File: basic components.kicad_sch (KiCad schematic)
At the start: 56 parts, among them U1601 74HC595, U1602 74HC165, U1603 ULN2803A, U1604 ULN2003A

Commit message: added ch340.sch
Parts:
- added Q?: AO3400A, Package_TO_SOT_SMD:SOT-23, symbol Transistor_FET:AO3400A
- D1606: footprint (none) -> Diode_SMD:D_SMA; JLCPCB Part# (none) -> C49264
- D1609: value (none) -> yellow_LED; footprint (none) -> LED_SMD:LED_0805_2012Metric_Pad1.15x1.40mm_HandSolder
- U?: value (none) -> EL817; footprint (none) -> Package_DIP:SMDIP-4_W9.53mm
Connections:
- net data_out: now also U1602.10 (DS)
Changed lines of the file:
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@@
   )
   (no_connect (at 189.23 31.75))
+  (wire (pts (xy 161.29 29.21) (xy 163.83 29.21))
+    (stroke (width 0) (type default) (color 0 0 0 0))
+  )
   (wire (pts (xy 232.41 55.88) (xy 232.41 57.15))
     (stroke (width 0) (type default) (color 0 0 0 0))
@@
       (effects (font (size 1.27 1.27)) (justify right))
     )
-    (property "Footprint" "" (id 2) (at 111.76 50.8 0)
+    (property "Footprint" "Diode_SMD:D_SMA" (id 2) (at 111.76 50.8 0)
       (effects (font (size 1.27 1.27)) hide)
     )
     (property "Datasheet" "~" (id 3) (at 111.76 50.8 0)
+      (effects (font (size 1.27 1.27)) hide)
+    )
+    (property "JLCPCB Part#" "C49264" (id 4) (at 111.76 50.8 90)
       (effects (font (size 1.27 1.27)) hide)
     )
@@
     (pin "1")
   )
+  (symbol (lib_id "Transistor_FET:AO3400A") (at 113.03 154.94 0) (unit 1)
+    (in_bom yes) (on_board yes) (fields_autoplaced)
+    (property "Reference" "Q?" (id 0) (at 118.237 154.1053 0)
+      (effects (font (size 1.27 1.27)) (justify left))
+    )
+    (property "Value" "AO3400A" (id 1) (at 118.237 156.6422 0)
+      (effects (font (size 1.27 1.27)) (justify left))
+    )
+    (property "Footprint" "Package_TO_SOT_SMD:SOT-23" (id 2) (at 118.11 156.845 0)
+      (effects (font (size 1.27 1.27) italic) (justify left) hide)
+    )
+    (property "Datasheet" "http://www.aosmd.com/pdfs/datasheet/AO3400A.pdf" (id 3) (at 113.03 154.94 0)
+      (effects (font (size 1.27 1.27)) (justify left) hide)
+    )
+    (property "JLCPCB Part#" "C20917" (id 4) (at 113.03 154.94 0)
+      (effects (font (size 1.27 1.27)) hide)
+    )
+    (pin "1")
+    (pin "2")
+    (pin "3")
+  )
   (symbol (lib_id "74xx:74HC595") (at 232.41 36.83 0) (unit 1)
     (in_bom yes) (on_board yes) (fields_autoplaced)
@@
     (in_bom yes) (on_board yes) (fields_autoplaced)
     (property "Reference" "U?" (id 0) (at 96.52 148.7002 0))
-    (property "Value" "" (id 1) (at 96.52 151.2371 0))
-    (property "Footprint" "" (id 2) (at 91.44 161.29 0)
+    (property "Value" "EL817" (id 1) (at 96.52 151.2371 0))
+    (property "Footprint" "Package_DIP:SMDIP-4_W9.53mm" (id 2) (at 91.44 161.29 0)
       (effects (font (size 1.27 1.27) italic) (justify left) hide)
     )
@@
       (effects (font (size 1.27 1.27)) (justify right))
     )
-    (property "Value" "" (id 1) (at 125.73 77.47 90)
-      (effects (font (size 1.27 1.27)) (justify right))
-    )
-    (property "Footprint" "" (id 2) (at 123.19 73.66 0)
-      (effects (font (size 1.27 1.27)) hide)
-    )
+    (property "Value" "yellow_LED" (id 1) (at 125.73 77.47 90)
+      (effects (font (size 1.27 1.27)) (justify right))
+    )
+    (property "Footprint" "LED_SMD:LED_0805_2012Metric_Pad1.15x1.40mm_HandSolder" (id 2) (at 123.19 73.66 0)
+      (effects (font (size 1.27 1.27)) hide)
+    )

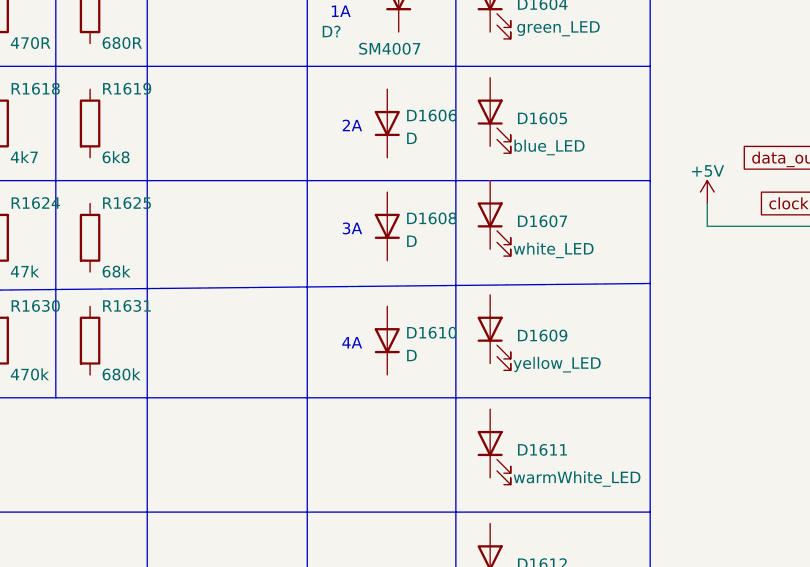
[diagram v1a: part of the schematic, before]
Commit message: added decoupling capacitor to atmega schematic
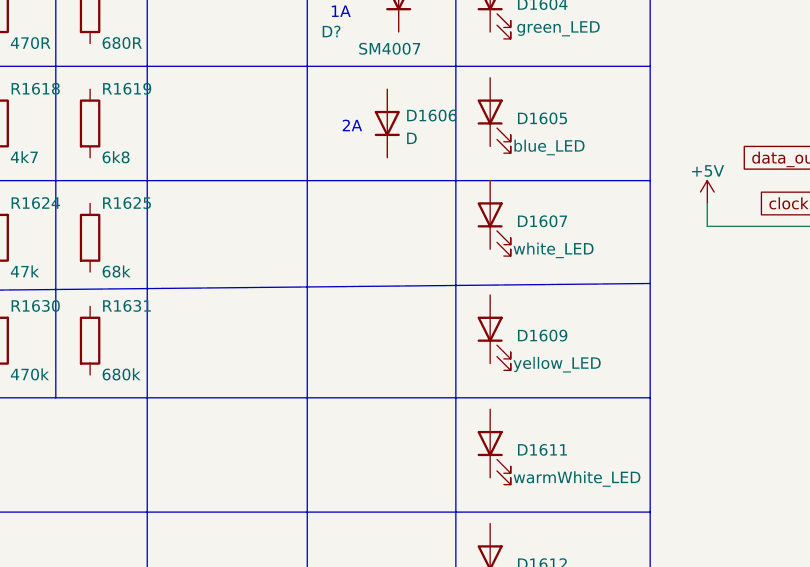
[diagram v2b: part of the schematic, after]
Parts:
- removed D1608, D1610: D, symbol Device:D
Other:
- note removed: "3A"
- note removed: "4A"
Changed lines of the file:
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@@
-    (effects (font (size 1.27 1.27)) (justify left bottom))
-  )
-  (text "3A" (at 106.68 63.5 0)
     (effects (font (size 1.27 1.27)) (justify left bottom))
   )
@@
   )
   (text "68" (at 78.74 16.51 0)
-    (effects (font (size 1.27 1.27)) (justify left bottom))
-  )
-  (text "4A" (at 106.68 76.2 0)
     (effects (font (size 1.27 1.27)) (justify left bottom))
   )
@@
     (pin "1")
   )
-  (symbol (lib_id "Device:D") (at 111.76 62.23 90) (unit 1)
-    (in_bom yes) (on_board yes) (fields_autoplaced)
-    (property "Reference" "D1608" (id 0) (at 113.792 61.3953 90)
-      (effects (font (size 1.27 1.27)) (justify right))
-    )
-    (property "Value" "D" (id 1) (at 113.792 63.9322 90)
-      (effects (font (size 1.27 1.27)) (justify right))
-    )
-    (property "Footprint" "" (id 2) (at 111.76 62.23 0)
-      (effects (font (size 1.27 1.27)) hide)
-    )
-    (property "Datasheet" "~" (id 3) (at 111.76 62.23 0)
-      (effects (font (size 1.27 1.27)) hide)
-    )
-    (pin "1")
-    (pin "2")
-  )
   (symbol (lib_id "Device:R") (at 38.1 25.4 0) (unit 1)
     (in_bom yes) (on_board yes)
@@
       (effects (font (size 1.27 1.27)) hide)
     )
-    (pin "1")
-    (pin "2")
-  )
-  (symbol (lib_id "Device:D") (at 111.76 74.93 90) (unit 1)
-    (in_bom yes) (on_board yes) (fields_autoplaced)
-    (property "Reference" "D1610" (id 0) (at 113.792 74.0953 90)
-      (effects (font (size 1.27 1.27)) (justify right))
-    )
-    (property "Value" "D" (id 1) (at 113.792 76.6322 90)
-      (effects (font (size 1.27 1.27)) (justify right))
-    )
-    (property "Footprint" "" (id 2) (at 111.76 74.93 0)
-      (effects (font (size 1.27 1.27)) hide)
-    )
-    (property "Datasheet" "~" (id 3) (at 111.76 74.93 0)
-      (effects (font (size 1.27 1.27)) hide)
-    )

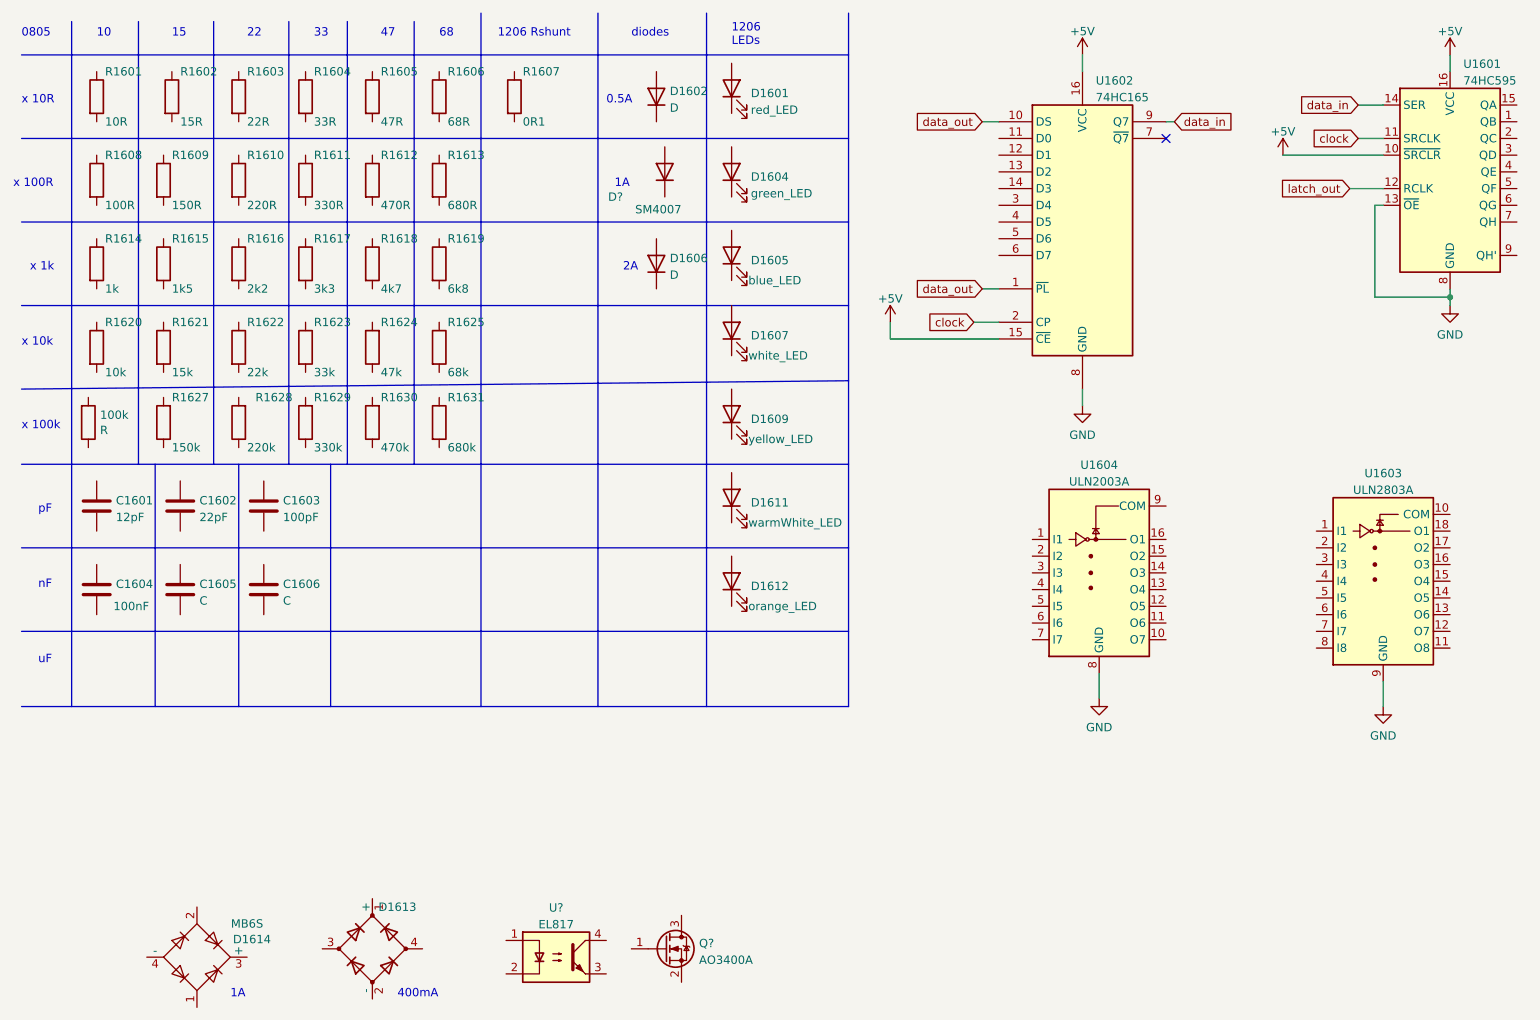
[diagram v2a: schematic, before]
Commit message: added hierarchial labels to some schematics
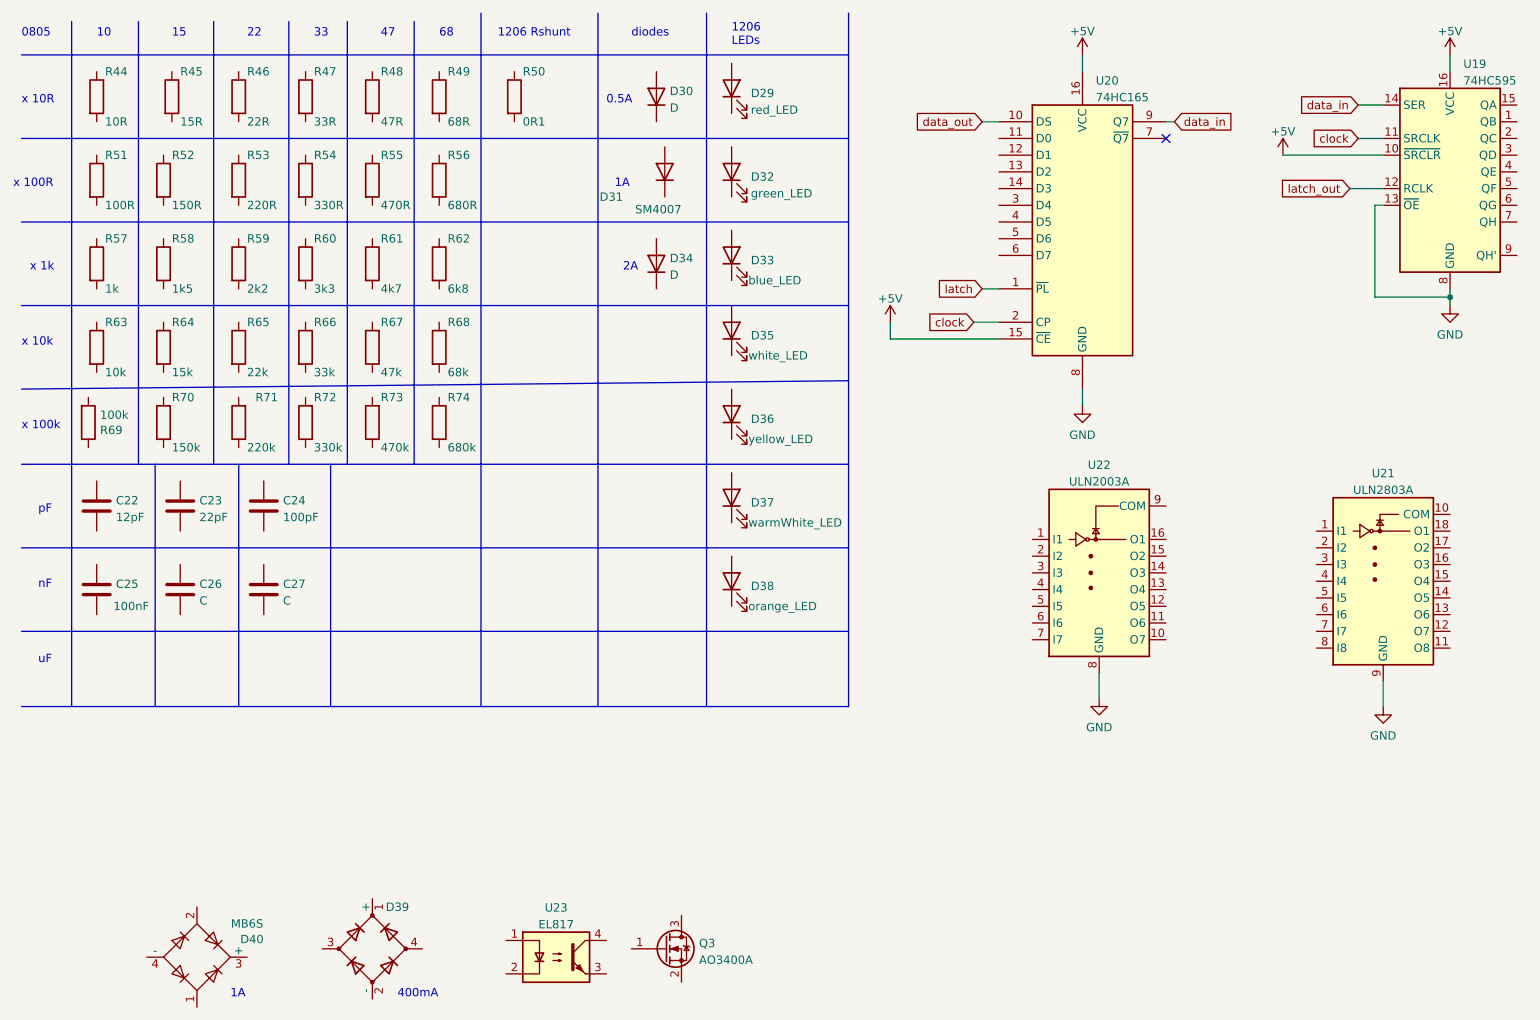
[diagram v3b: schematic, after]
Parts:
- gave numbers to parts that had none: 3
- renumbered C1601 to C22, C1602 to C23, C1603 to C24, C1604 to C25, C1605 to C26, C1606 to C27, D1601 to D29, D1602 to D30, D1604 to D32, D1605 to D33, D1606 to D34, D1607 to D35, D1609 to D36, D1611 to D37, D1612 to D38, D1613 to D39, D1614 to D40, R1601 to R44, R1602 to R45, R1603 to R46, R1604 to R47, R1605 to R48, R1606 to R49, R1607 to R50, R1608 to R51, R1609 to R52, R1610 to R53, R1611 to R54, R1612 to R55, R1613 to R56, R1614 to R57, R1615 to R58, R1616 to R59, R1617 to R60, R1618 to R61, R1619 to R62, R1620 to R63, R1621 to R64, R1622 to R65, R1623 to R66, R1624 to R67, R1625 to R68, R to R69, R1627 to R70, R1628 to R71, R1629 to R72, R1630 to R73, R1631 to R74, U1601 to U19, U1602 to U20, U1603 to U21, U1604 to U22
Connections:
- net data_out: no longer U20.1 (~{PL})
- new net latch: U20.1 (~{PL})

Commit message: moved some schematic scheets to their own folders and routed a board with it. This allow for re-use of PCB parts.
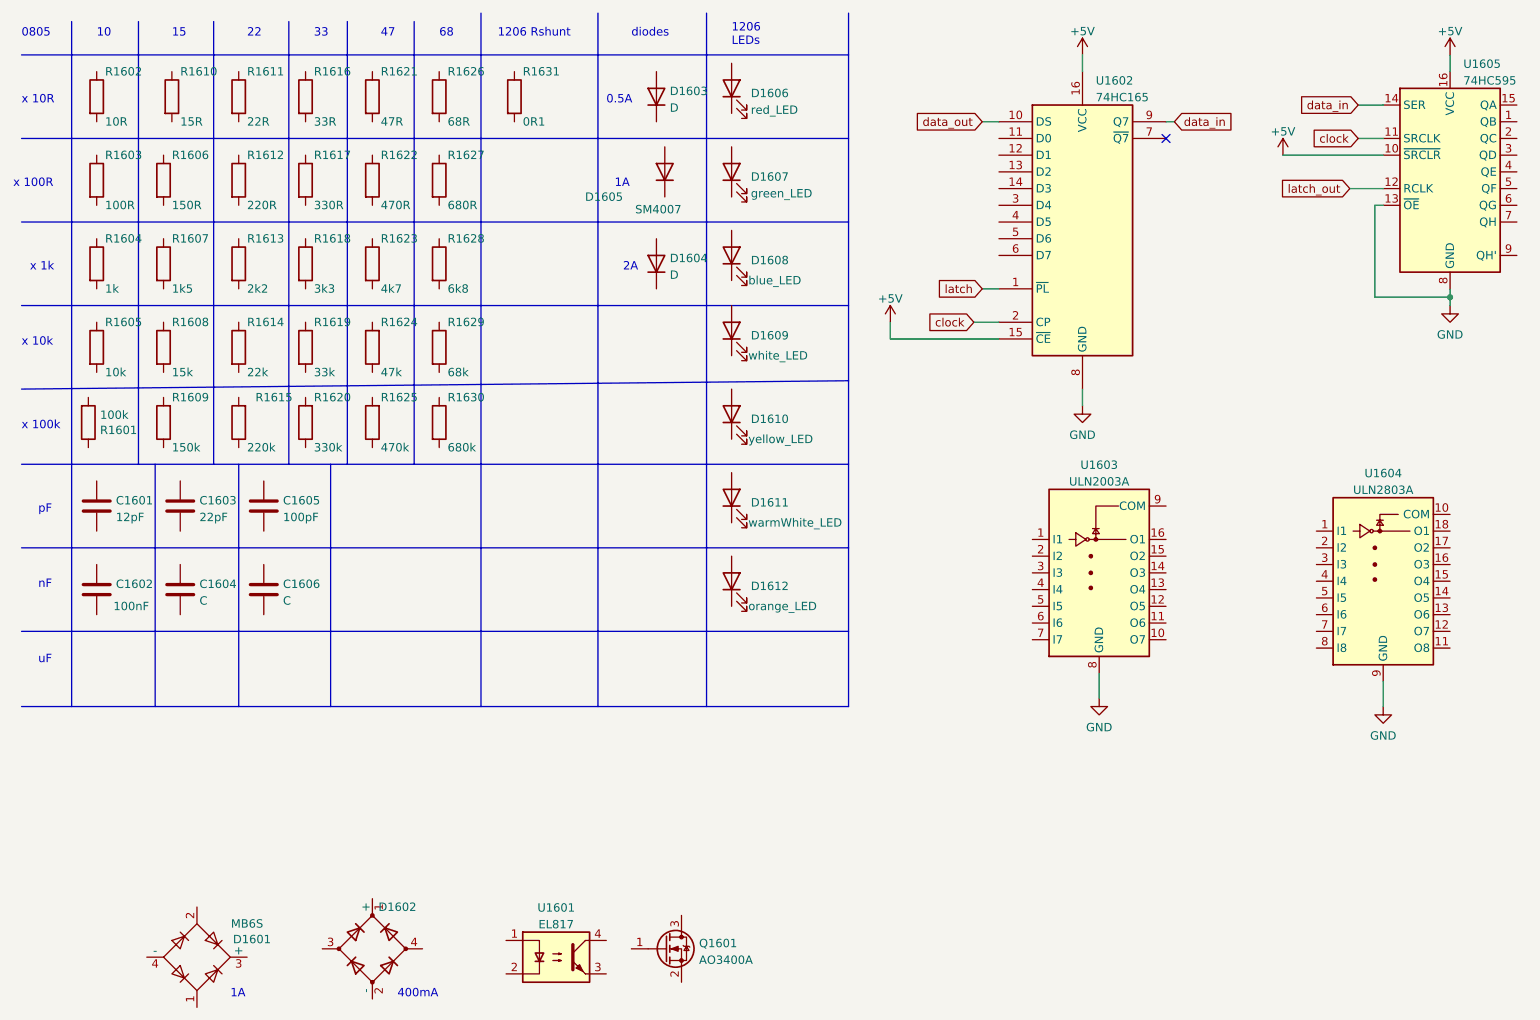
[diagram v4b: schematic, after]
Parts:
- renumbered C22 to C1601, C25 to C1602, C23 to C1603, C26 to C1604, C24 to C1605, C27 to C1606, D40 to D1601, D39 to D1602, D30 to D1603, D34 to D1604, D31 to D1605, D29 to D1606, D32 to D1607, D33 to D1608, D35 to D1609, D36 to D1610, D37 to D1611, D38 to D1612, Q3 to Q1601, R69 to R1601, R44 to R1602, R51 to R1603, R57 to R1604, R63 to R1605, R52 to R1606, R58 to R1607, R64 to R1608, R70 to R1609, R45 to R1610, R46 to R1611, R53 to R1612, R59 to R1613, R65 to R1614, R71 to R1615, R47 to R1616, R54 to R1617, R60 to R1618, R66 to R1619, R72 to R1620, R48 to R1621, R55 to R1622, R61 to R1623, R67 to R1624, R73 to R1625, R49 to R1626, R56 to R1627, R62 to R1628, R68 to R1629, R74 to R1630, R50 to R1631, U23 to U1601, U20 to U1602, U22 to U1603, U21 to U1604, U19 to U1605
